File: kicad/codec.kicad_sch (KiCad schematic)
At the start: 0 parts

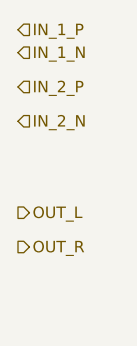
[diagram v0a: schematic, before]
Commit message: added TXE8124 and THAT5263
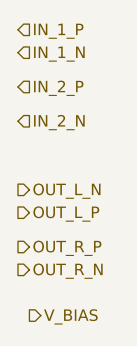
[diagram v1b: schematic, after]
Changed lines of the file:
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@@
 	(generator_version "9.0")
 	(paper "A4")
+	(hierarchical_label "OUT_R_N"
+		(shape output)
+		(at 246.38 81.28 0)
+		(effects
+			(font
+				(size 1.27 1.27)
+			)
+			(justify left)
+		)
+	)
 	(hierarchical_label "IN_2_N"
 		(shape input)
@@
 		)
 	)
+	(hierarchical_label "V_BIAS"
+		(shape output)
+		(at 247.65 86.36 0)
+		(effects
+			(font
+				(size 1.27 1.27)
+			)
+			(justify left)
+		)
+	)
 	(hierarchical_label "IN_1_P"
 		(shape input)
@@
 		)
 	)
-	(hierarchical_label "OUT_R"
+	(hierarchical_label "OUT_L_N"
+		(shape output)
+		(at 246.38 72.39 0)
+		(effects
+			(font
+				(size 1.27 1.27)
+			)
+			(justify left)
+		)
+	)
+	(hierarchical_label "OUT_R_P"
 		(shape output)
 		(at 246.38 78.74 0)
@@
 		)
 	)
-	(hierarchical_label "OUT_L"
+	(hierarchical_label "OUT_L_P"
 		(shape output)
 		(at 246.38 74.93 0)

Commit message: tac5212 initial architecture
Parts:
- added C63, C74, C80: 100nF, symbol Device:C_Small
- added C69, C71, C75: 10uF, symbol Device:C_Small
- added C70: 1uF, symbol Device:C_Small
- added U11: TAC5212, symbol openmic:TAC5212
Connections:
- net IN_1_N: now also U11.16 (IN1M)
- net IN_1_P: now also U11.15 (IN1P)
- net IN_2_N: now also U11.18 (IN2M)
- net IN_2_P: now also U11.17 (IN2P)
- net V_BIAS: now also U11.14 (MICBIAS)
- new net: C71.1, C74.1, U11.1 (DREG)
- new net: C70.2, U11.24 (VREF)
- new net +3V3: C63.2, C69.2, C75.1, C80.1, U11.23 (AVDD), U11.6 (IOVDD)
- new net BCLK: U11.2 (BCLK)
- new net DIN: U11.5 (DIN)
- new net DOUT: U11.4 (DOUT)
- new net FSYNC: U11.3 (FSYNC)
- new net GNDD: C63.1, C69.1, C70.1, C71.2, C74.2, C75.2, C80.2, U11.0 (PAD), U11.13 (ADDR), U11.A1 (VSS), U11.A2 (VSS), U11.A3 (VSS), U11.A4 (VSS)
- new net GPIO1: U11.9 (GPIO1)
- new net GPIO2: U11.10 (GPIO2)
- new net OUT_LINE_L: U11.21 (OUT2P)
- new net OUT_LINE_R: U11.22 (OUT2M)
- new net OUT_PHONE_L: U11.20 (OUT1P)
- new net OUT_PHONE_R: U11.19 (OUT1M)
- new net SPI_CS: U11.12 (GPI1)
- new net SPI_PICO: U11.8 (SDA)
- new net SPI_POCI: U11.11 (GPO1)
- new net SPI_SCLK: U11.7 (SCL)

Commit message: #13
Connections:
- net GPIO1 renamed CCLK
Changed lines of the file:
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@@
 		)
 	)
-	(hierarchical_label "GPIO1"
-		(shape bidirectional)
+	(hierarchical_label "CCLK"
+		(shape input)
 		(at 109.22 120.65 270)
 		(effects

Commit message: external power supply (#9)
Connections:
- net GPIO2 renamed GPIO_2
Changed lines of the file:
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@@
 		)
 	)
-	(hierarchical_label "GPIO2"
+	(hierarchical_label "GPIO_2"
 		(shape bidirectional)
 		(at 106.68 120.65 270)

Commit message: CH224K external supply
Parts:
- renumbered C71 to C80, C69 to C81, C70 to C82, C74 to C83, C63 to C84, C75 to C85, C80 to C86
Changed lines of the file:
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@@
 		(dnp no)
 		(fields_autoplaced yes)
-		(property "Reference" "C74"
+		(property "Reference" "C83"
 			(at 139.7063 50.8 90)
 			(effects
@@
 			(project "openmic"
 				(path "/84faeadc-8b12-4a66-a17f-5c56e5923fb8/48193676-4a40-49fd-9b42-70b8319c374b"
-					(reference "C74")
+					(reference "C83")
 					(unit 1)
 				)
@@
 		(dnp no)
 		(fields_autoplaced yes)
-		(property "Reference" "C75"
+		(property "Reference" "C85"
 			(at 165.1063 53.34 90)
 			(effects
@@
 			(project "openmic"
 				(path "/84faeadc-8b12-4a66-a17f-5c56e5923fb8/48193676-4a40-49fd-9b42-70b8319c374b"
-					(reference "C75")
+					(reference "C85")
 					(unit 1)
 				)
@@
 		(dnp no)
 		(fields_autoplaced yes)
-		(property "Reference" "#PWR0138"
+		(property "Reference" "#PWR0118"
 			(at 173.99 76.2 0)
 			(effects
@@
 			(project "openmic"
 				(path "/84faeadc-8b12-4a66-a17f-5c56e5923fb8/48193676-4a40-49fd-9b42-70b8319c374b"
-					(reference "#PWR0138")
+					(reference "#PWR0118")
 					(unit 1)
 				)
@@
 		(dnp no)
 		(fields_autoplaced yes)
-		(property "Reference" "#PWR071"
+		(property "Reference" "#PWR0120"
 			(at 149.86 116.84 0)
 			(effects
@@
 			(project "openmic"
 				(path "/84faeadc-8b12-4a66-a17f-5c56e5923fb8/48193676-4a40-49fd-9b42-70b8319c374b"
-					(reference "#PWR071")
+					(reference "#PWR0120")
 					(unit 1)
 				)
@@
 		(dnp no)
 		(fields_autoplaced yes)
-		(property "Reference" "#PWR0126"
+		(property "Reference" "#PWR0115"
 			(at 124.46 64.77 0)
 			(effects
@@
 			(project "openmic"
 				(path "/84faeadc-8b12-4a66-a17f-5c56e5923fb8/48193676-4a40-49fd-9b42-70b8319c374b"
-					(reference "#PWR0126")
+					(reference "#PWR0115")
 					(unit 1)
 				)
@@
 		(dnp no)
 		(fields_autoplaced yes)
-		(property "Reference" "#PWR068"
+		(property "Reference" "#PWR0119"
 			(at 83.82 81.28 0)
 			(effects
@@
 			(project "openmic"
 				(path "/84faeadc-8b12-4a66-a17f-5c56e5923fb8/48193676-4a40-49fd-9b42-70b8319c374b"
-					(reference "#PWR068")
+					(reference "#PWR0119")
 					(unit 1)
 				)
@@
 		(dnp no)
 		(fields_autoplaced yes)
-		(property "Reference" "#PWR072"
+		(property "Reference" "#PWR0114"
 			(at 101.6 45.72 0)
 			(effects
@@
 			(project "openmic"
 				(path "/84faeadc-8b12-4a66-a17f-5c56e5923fb8/48193676-4a40-49fd-9b42-70b8319c374b"
-					(reference "#PWR072")
+					(reference "#PWR0114")
 					(unit 1)
 				)
@@
 		(dnp no)
 		(fields_autoplaced yes)
-		(property "Reference" "C71"
+		(property "Reference" "C80"
 			(at 139.7063 39.37 90)
 			(effects
@@
 			(project "openmic"
 				(path "/84faeadc-8b12-4a66-a17f-5c56e5923fb8/48193676-4a40-49fd-9b42-70b8319c374b"
-					(reference "C71")
+					(reference "C80")
 					(unit 1)
 				)
@@
 		(dnp no)
 		(fields_autoplaced yes)
-		(property "Reference" "#PWR0134"
+		(property "Reference" "#PWR0116"
 			(at 147.32 64.77 0)
 			(effects
@@
 			(project "openmic"
 				(path "/84faeadc-8b12-4a66-a17f-5c56e5923fb8/48193676-4a40-49fd-9b42-70b8319c374b"
-					(reference "#PWR0134")
+					(reference "#PWR0116")
 					(unit 1)
 				)
@@
 		(dnp no)
 		(fields_autoplaced yes)
-		(property "Reference" "C69"
+		(property "Reference" "C81"
 			(at 93.9863 40.64 90)
 			(effects
@@
 			(project "openmic"
 				(path "/84faeadc-8b12-4a66-a17f-5c56e5923fb8/48193676-4a40-49fd-9b42-70b8319c374b"
-					(reference "C69")
+					(reference "C81")
 					(unit 1)
 				)
@@
 		(dnp no)
 		(fields_autoplaced yes)
-		(property "Reference" "#PWR0135"
+		(property "Reference" "#PWR0117"
 			(at 156.21 63.5 0)
 			(effects
@@
 			(project "openmic"
 				(path "/84faeadc-8b12-4a66-a17f-5c56e5923fb8/48193676-4a40-49fd-9b42-70b8319c374b"
-					(reference "#PWR0135")
+					(reference "#PWR0117")
 					(unit 1)
 				)
@@
 		(dnp no)
 		(fields_autoplaced yes)
-		(property "Reference" "C80"
+		(property "Reference" "C86"
 			(at 165.1063 63.5 90)
 			(effects
@@
 			(project "openmic"
 				(path "/84faeadc-8b12-4a66-a17f-5c56e5923fb8/48193676-4a40-49fd-9b42-70b8319c374b"
-					(reference "C80")
+					(reference "C86")
 					(unit 1)
 				)
@@
 		(dnp no)
 		(fields_autoplaced yes)
-		(property "Reference" "C63"
+		(property "Reference" "C84"
 			(at 93.9863 52.07 90)
 			(effects
@@
 			(project "openmic"
 				(path "/84faeadc-8b12-4a66-a17f-5c56e5923fb8/48193676-4a40-49fd-9b42-70b8319c374b"
-					(reference "C63")
+					(reference "C84")
 					(unit 1)
 				)
@@
 		(dnp no)
 		(fields_autoplaced yes)
-		(property "Reference" "C70"
+		(property "Reference" "C82"
 			(at 120.6436 50.8 90)
 			(effects
@@
 			(project "openmic"
 				(path "/84faeadc-8b12-4a66-a17f-5c56e5923fb8/48193676-4a40-49fd-9b42-70b8319c374b"
-					(reference "C70")
-					(unit 1)
-				)
+					(reference "C82")
+					(unit 1)
+				)
